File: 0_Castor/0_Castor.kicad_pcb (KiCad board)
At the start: 2 copper layers, 138.3 x 176.1 mm, 94 parts, among them J1 Conn_01x02, SW1 Battery Switch, SW2 Reset Switch, U1 Nice_Nano_V2

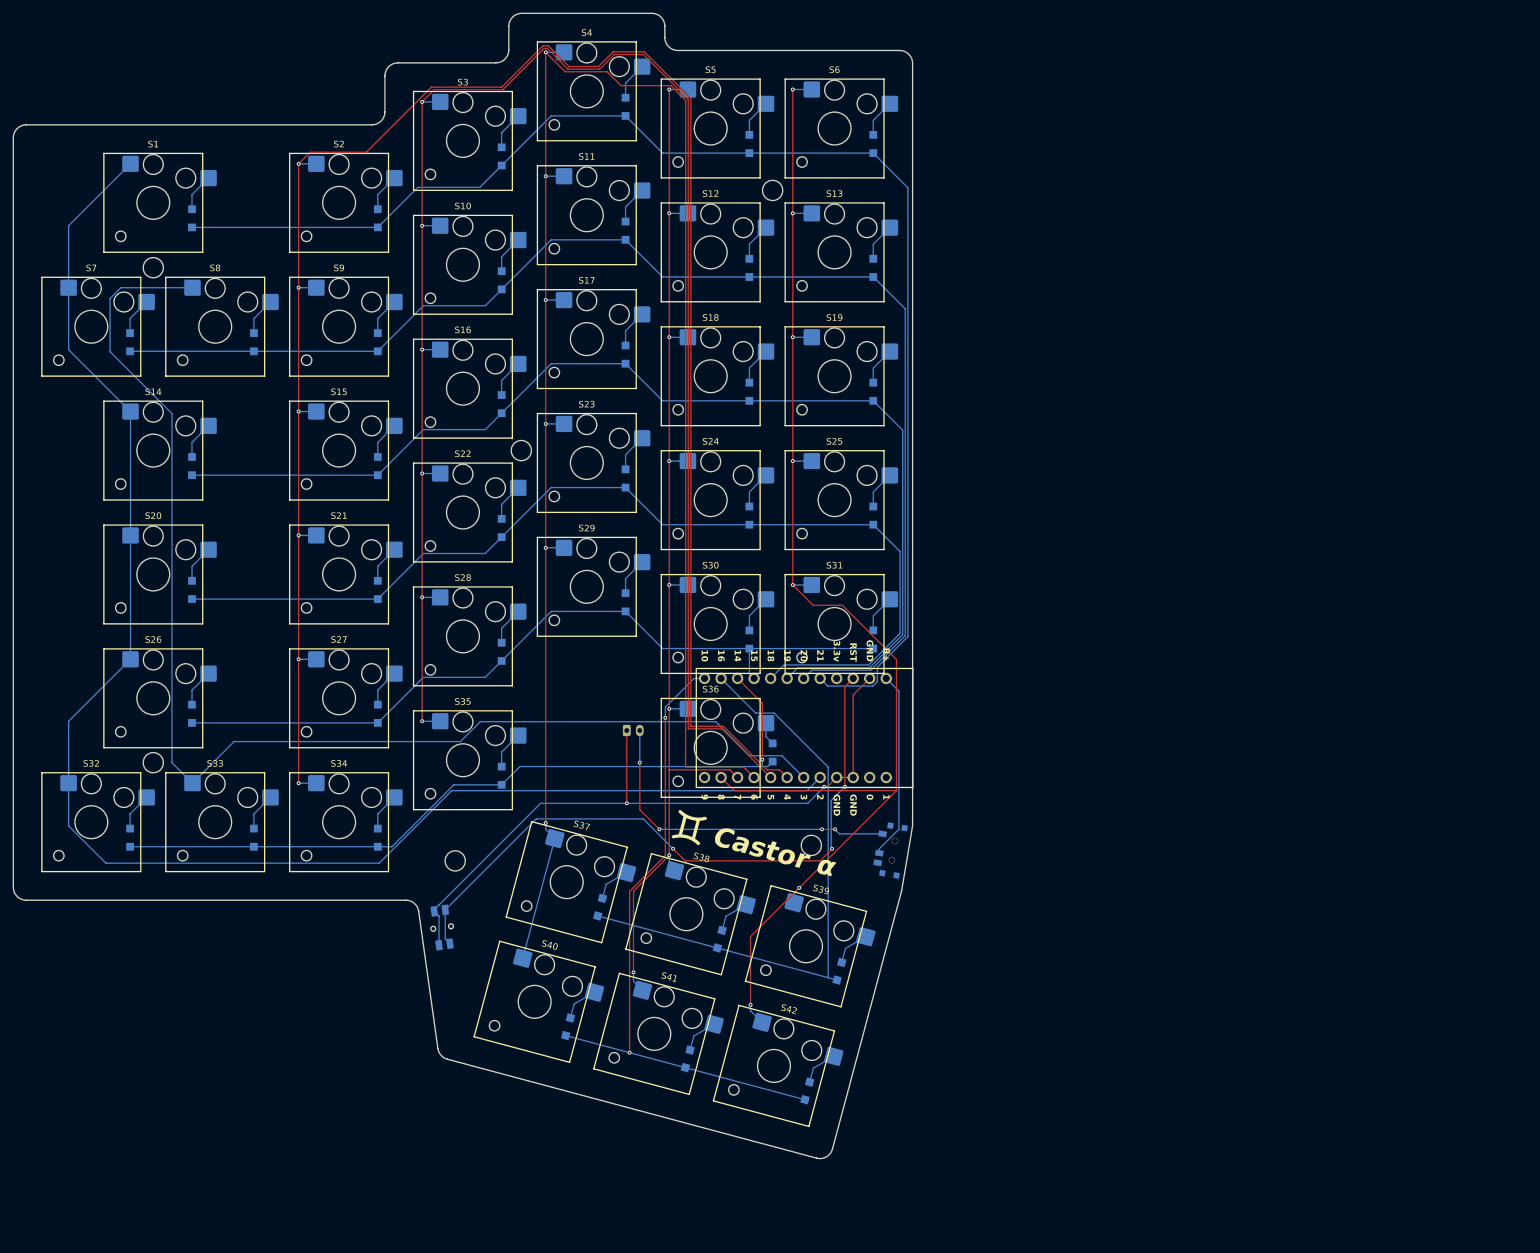
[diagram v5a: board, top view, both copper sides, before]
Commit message: feat: finish Pollux PCB | chore: generate gerber files for both sides
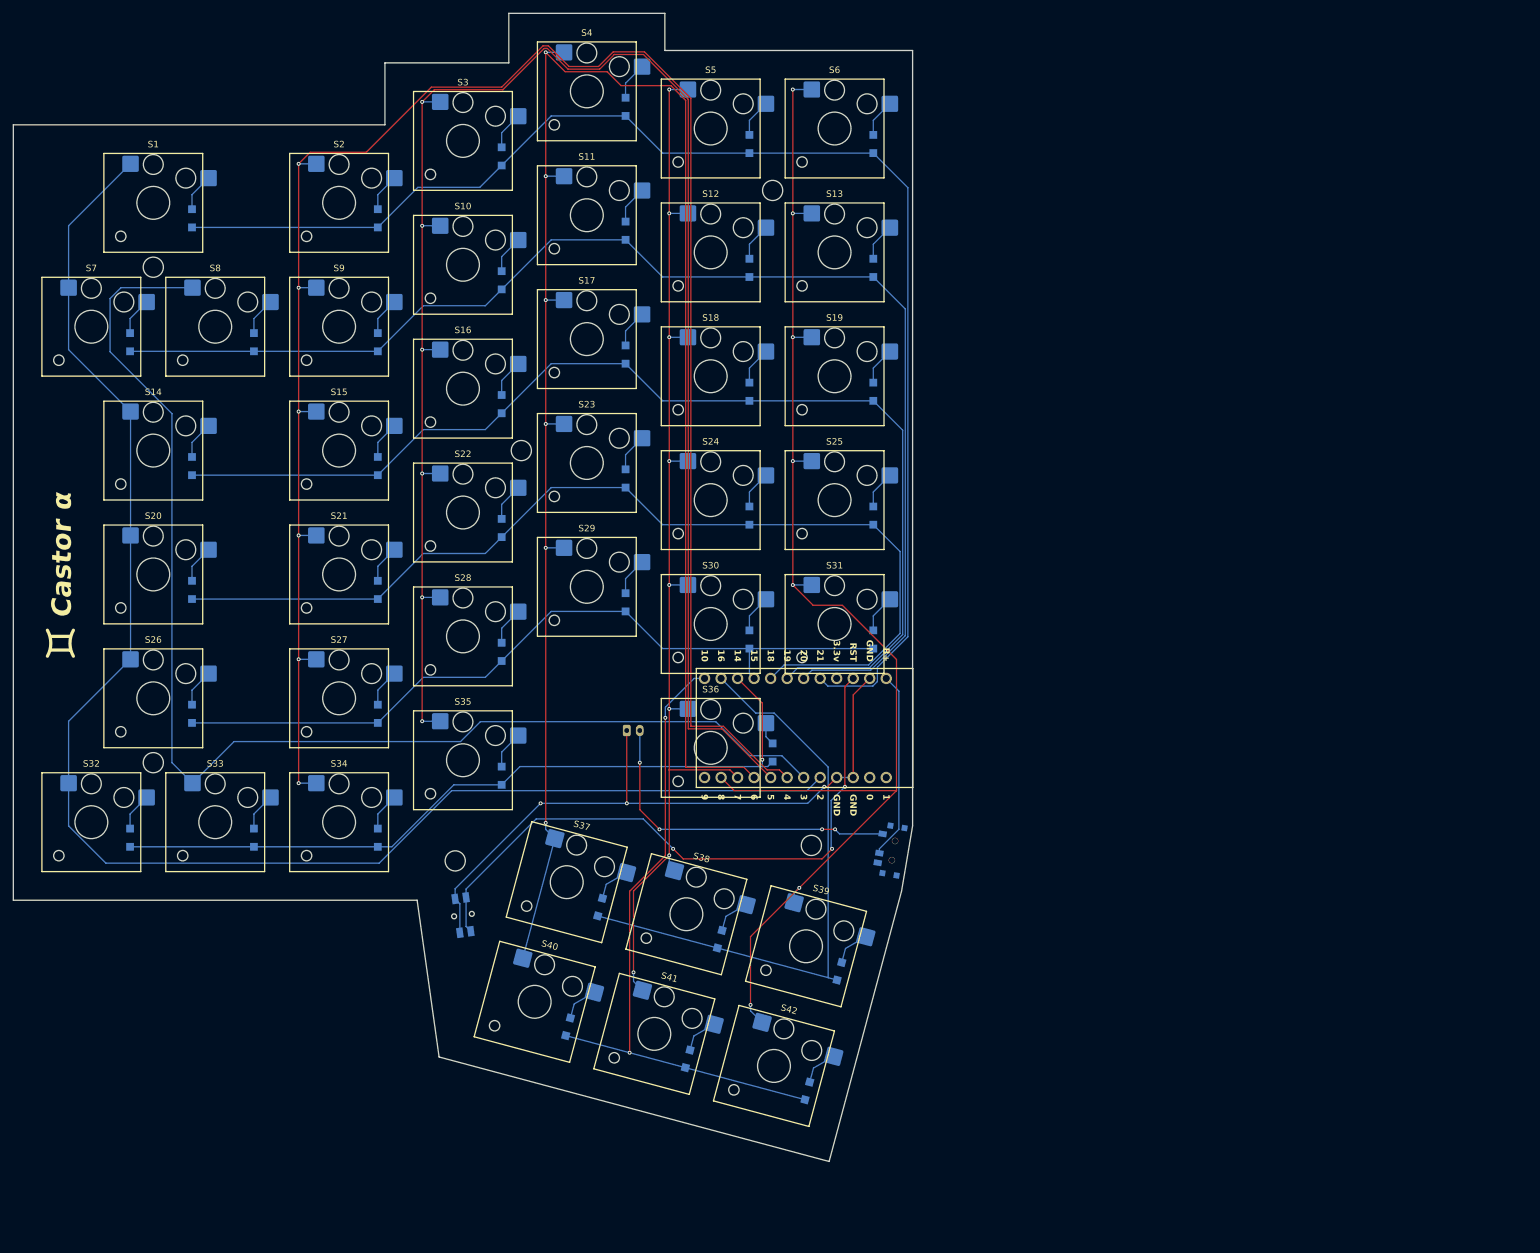
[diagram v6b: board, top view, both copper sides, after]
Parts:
- moved SW2 3.73 mm to (104.8, 166.7)
- moved REF** 0.08 mm to (57.1, 67.0)
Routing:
- net /RST: track 101.9 -> 98.4 mm
- net GND: track 106.1 -> 102.9 mm, vias 2 -> 3
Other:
- board size 138.3 x 176.1 mm -> 138.3 x 176.6 mm
